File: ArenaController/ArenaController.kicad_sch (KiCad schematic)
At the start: 29 parts, among them J1 RJ45, J2 RJ45, J4 RJ45, J5 RJ45, J6 RJ45, J8 Screw_Terminal_01x04, J9 Barrel_Jack_MountingPin, Q1 FS3400, Q2 FS3400, Q3 FS3400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

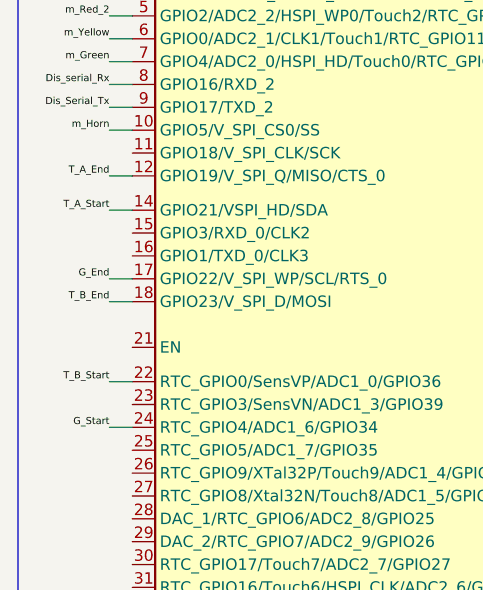
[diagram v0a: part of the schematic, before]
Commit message: Revision .4 layout with a sane ground plane, do fix the footprint shit tho
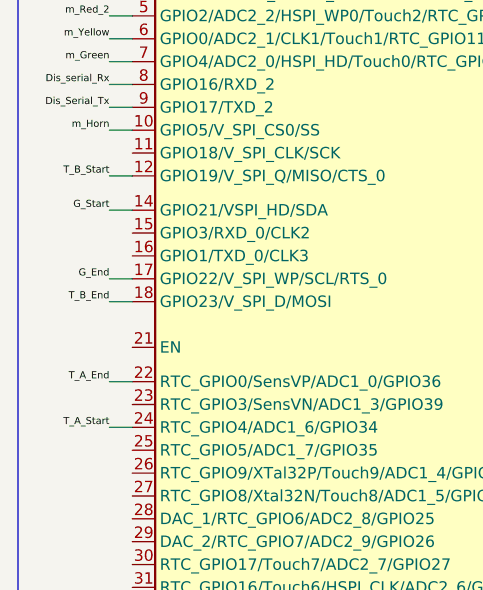
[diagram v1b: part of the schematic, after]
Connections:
- net G_Start: now also U3.14 (GPIO21/VSPI_HD/SDA); no longer U3.24 (RTC_GPIO4/ADC1_6/GPIO34)
- net T_A_End: now also U3.22 (RTC_GPIO0/SensVP/ADC1_0/GPIO36); no longer U3.12 (GPIO19/V_SPI_Q/MISO/CTS_0)
- net T_A_Start: now also U3.24 (RTC_GPIO4/ADC1_6/GPIO34); no longer U3.14 (GPIO21/VSPI_HD/SDA)
- net T_B_Start: now also U3.12 (GPIO19/V_SPI_Q/MISO/CTS_0); no longer U3.22 (RTC_GPIO0/SensVP/ADC1_0/GPIO36)

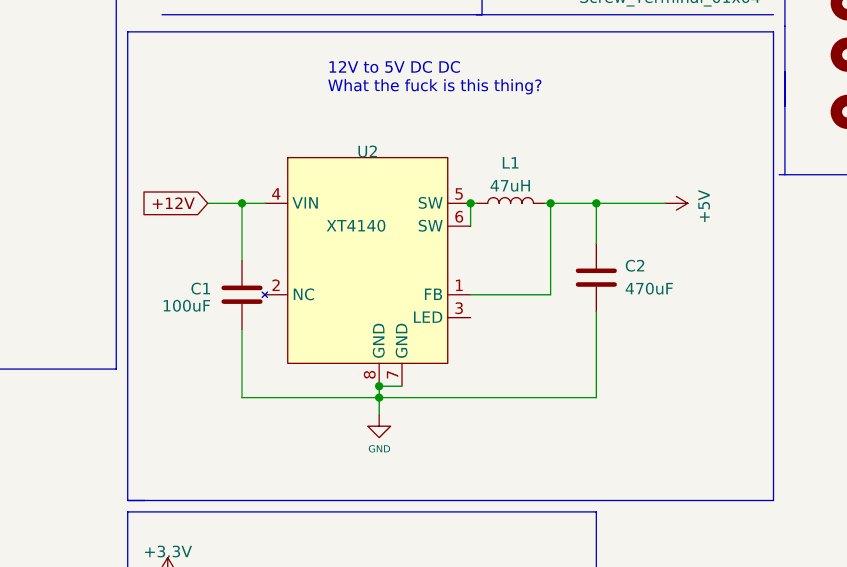
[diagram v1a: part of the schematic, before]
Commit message: Work day fixes for schematic, including re-polarizing the caps.
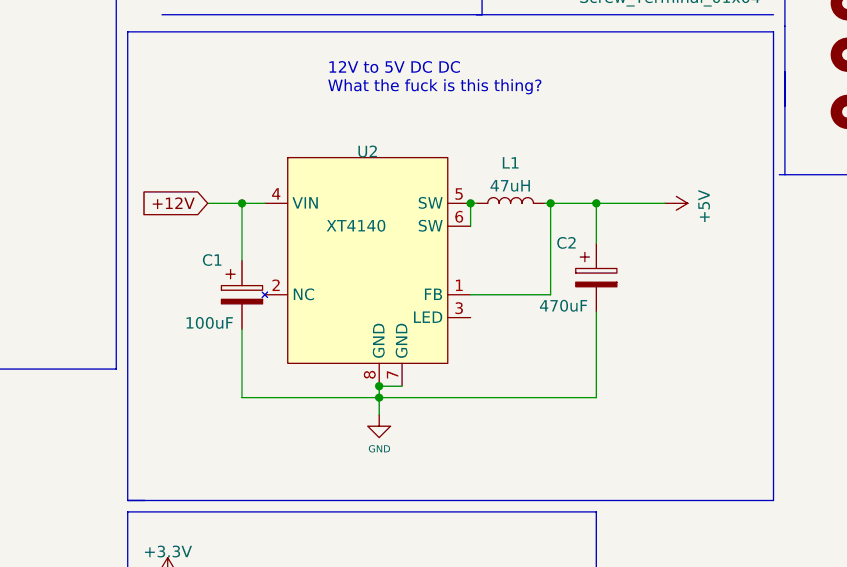
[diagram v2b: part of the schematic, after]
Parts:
- removed C1: 100uF, Capacitor_SMD:C_Elec_6.3x5.4, symbol Device:C
- removed C2: 470uF, Capacitor_SMD:C_Elec_6.3x7.7, symbol Device:C
- added C1: 100uF, Capacitor_SMD:C_Elec_6.3x5.4, symbol Device:C_Polarized
- added C2: 470uF, Capacitor_SMD:C_Elec_6.3x5.4, symbol Device:C_Polarized
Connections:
- net +12V: now also C1.1
- net +5V: now also C2.1
- net GND: now also C1.2, C2.2
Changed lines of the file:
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@@
   (title_block
     (title "Combat Arena Timing Control")
-    (date "2023-03-21")
-    (rev "0.4")
+    (date "2023-04-13")
+    (rev "0.4a")
     (company "Fair Use Building & Research Labs, 501c3")
     (comment 2 "Neil Flynn")
@@
     )
   )
-  (symbol (lib_id "Device:C") (at 166.37 132.08 180) (unit 1)
-    (in_bom yes) (on_board yes) (dnp no)
-    (property "Reference" "C2" (at 169.545 130.81 0)
-      (effects (font (size 1.27 1.27)) (justify right))
-    )
-    (property "Value" "470uF" (at 169.545 133.35 0)
-      (effects (font (size 1.27 1.27)) (justify right))
-    )
-    (property "Footprint" "Capacitor_SMD:C_Elec_6.3x7.7" (at 165.4048 128.27 0)
-      (effects (font (size 1.27 1.27)) hide)
-    )
-    (property "Datasheet" "https://datasheet.lcsc.com/lcsc/2202231130_ROQANG-RVT1C471M0607_C2977552.pdf" (at 166.37 132.08 0)
-      (effects (font (size 1.27 1.27)) hide)
-    )
-    (property "LCSC" "https://www.lcsc.com/product-detail/Aluminum-Electrolytic-Capacitors-SMD_ROQANG-RVT1C471M0607_C2977552.html" (at 166.37 132.08 0)
-      (effects (font (size 1.27 1.27)) hide)
-    )
-    (pin "1")
-    (pin "2")
-    (instances
-      (project "ArenaController"
-        (path "/156576da-4c7a-4c71-af43-7540e3a24bd3"
-          (reference "C2") (unit 1)
+  (symbol (lib_id "Device:C_Polarized") (at 127 133.985 0) (unit 1)
+    (in_bom yes) (on_board yes) (dnp no)
+    (property "Reference" "C1" (at 122.555 130.175 0)
+      (effects (font (size 1.27 1.27)) (justify left))
+    )
+    (property "Value" "100uF" (at 120.65 137.16 0)
+      (effects (font (size 1.27 1.27)) (justify left))
+    )
+    (property "Footprint" "Capacitor_SMD:C_Elec_6.3x5.4" (at 127.9652 137.795 0)
+      (effects (font (size 1.27 1.27)) hide)
+    )
+    (property "Datasheet" "~" (at 127 133.985 0)
+      (effects (font (size 1.27 1.27)) hide)
+    )
+    (pin "1")
+    (pin "2")
+    (instances
+      (project "ArenaController"
+        (path "/156576da-4c7a-4c71-af43-7540e3a24bd3"
+          (reference "C1") (unit 1)
         )
       )
@@
     )
   )
-  (symbol (lib_id "Device:C") (at 127 133.985 180) (unit 1)
-    (in_bom yes) (on_board yes) (dnp no)
-    (property "Reference" "C1" (at 121.285 133.35 0)
-      (effects (font (size 1.27 1.27)) (justify right))
-    )
-    (property "Value" "100uF" (at 118.11 135.255 0)
-      (effects (font (size 1.27 1.27)) (justify right))
-    )
-    (property "Footprint" "Capacitor_SMD:C_Elec_6.3x5.4" (at 126.0348 130.175 0)
-      (effects (font (size 1.27 1.27)) hide)
-    )
-    (property "Datasheet" "https://datasheet.lcsc.com/lcsc/2207221830_KNSCHA-RST100UF25V004_C4747964.pdf" (at 127 133.985 0)
-      (effects (font (size 1.27 1.27)) hide)
-    )
-    (property "LCSC" "https://www.lcsc.com/product-detail/Aluminum-Electrolytic-Capacitors-SMD_KNSCHA-RST100UF25V004_C4747964.html" (at 127 133.985 0)
-      (effects (font (size 1.27 1.27)) hide)
-    )
-    (pin "1")
-    (pin "2")
-    (instances
-      (project "ArenaController"
-        (path "/156576da-4c7a-4c71-af43-7540e3a24bd3"
-          (reference "C1") (unit 1)
-        )
-      )
+  (symbol (lib_id "Device:C_Polarized") (at 166.37 132.08 0) (unit 1)
+    (in_bom yes) (on_board yes) (dnp no)
+    (property "Reference" "C2" (at 161.925 128.27 0)
+      (effects (font (size 1.27 1.27)) (justify left))
+    )
+    (property "Value" "470uF" (at 160.02 135.255 0)
+      (effects (font (size 1.27 1.27)) (justify left))
+    )
+    (property "Footprint" "Capacitor_SMD:C_Elec_6.3x5.4" (at 167.3352 135.89 0)
+      (effects (font (size 1.27 1.27)) hide)
+    )
+    (property "Datasheet" "https://datasheet.lcsc.com/lcsc/2202231130_ROQANG-RVT1C471M0607_C2977552.pdf" (at 166.37 132.08 0)
+      (effects (font (size 1.27 1.27)) hide)
+    )
+    (property "LCSC" "https://www.lcsc.com/product-detail/Aluminum-Electrolytic-Capacitors-SMD_ROQANG-RVT1C471M0607_C2977552.html" (at 166.37 132.08 0)
+      (effects (font (size 1.27 1.27)) hide)
+    )
+    (pin "1")
+    (pin "2")
+    (instances
+      (project "ArenaController"
+        (path "/156576da-4c7a-4c71-af43-7540e3a24bd3"
+          (reference "C2") (unit 1)
+        )
+      )

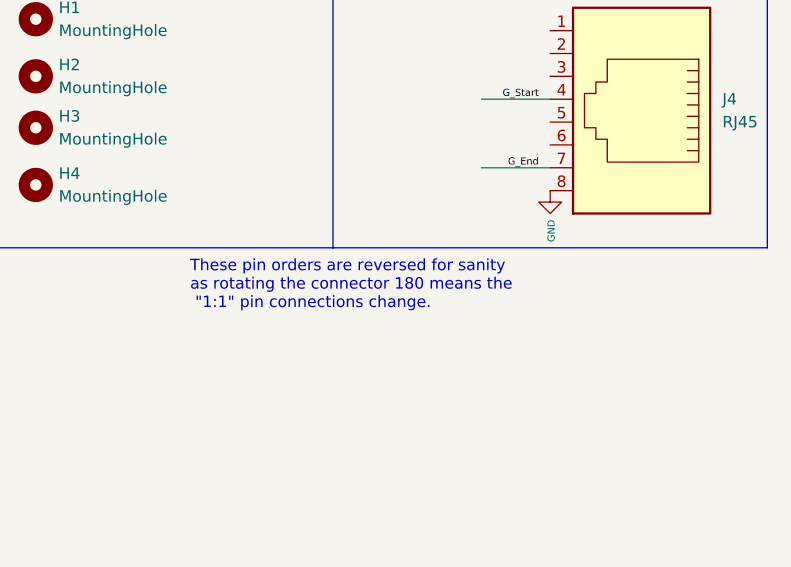
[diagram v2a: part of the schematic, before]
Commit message: Added SPIFFS note for if we need to use embedded FS stuff.  Yay!
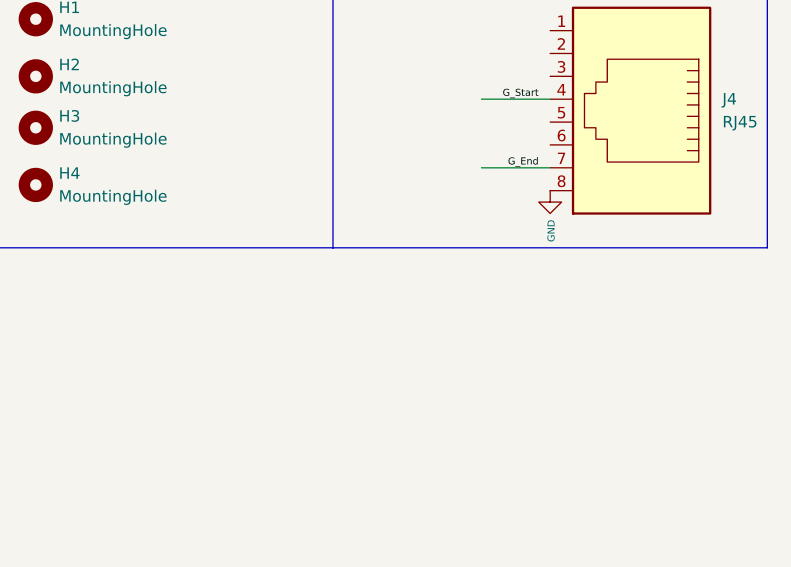
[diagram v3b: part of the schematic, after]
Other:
- note removed: "These pin orders are reversed for sanity as rotating the connector 180 means the "1:1" pin connections change."
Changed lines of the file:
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@@
   (title_block
     (title "Combat Arena Timing Control")
-    (date "2023-04-13")
+    (date "2023-04-14")
     (rev "0.4a")
     (company "Fair Use Building & Research Labs, 501c3")
@@
     (effects (font (size 1.27 1.27)) (justify left bottom))
   )
-  (text "These pin orders are reversed for sanity\nas rotating the connector 180 means the\n \"1:1\" pin connections change."
-    (at 211.455 127.635 0)
-    (effects (font (size 1.27 1.27)) (justify left bottom))
-  )
